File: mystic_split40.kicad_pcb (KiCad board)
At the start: 2 copper layers, 200.5 x 98.8 mm, 152 parts, among them J1 RX, J15 RESET, J16 ISP, J17 WS2812, J18 SJ-43514-SMT, J2 TX, J25 TYPE-C-31-M-12, J3 RX, J33 RESET, J34 ISP, J35 WS2812, J36 SJ-43514-SMT, J5 TX, J7 TYPE-C-31-M-12, SW1 EC11E, SW2 EC11E, SW3 Reset, SW4 Reset, U1 ATmega32U4-AU, U2 ATmega32U4-AU, Y1 CSTNE16M0VH3L000R0, Y2 CSTNE16M0VH3L000R0

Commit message: Swapped SDA and SCL pins on TRRS jack
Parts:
- removed C7, C8: 4.7nF, Capacitor_SMD:C_0603_1608Metric_Pad1.05x0.95mm_HandSolder
- removed R25, R26: 1M, Resistor_SMD:R_0603_1608Metric_Pad1.05x0.95mm_HandSolder
- added J4: F0, TestPoint:TestPoint_Pad_D1.0mm, B.Cu at (64.3, 21.5)
- added J6: F1, TestPoint:TestPoint_Pad_D1.0mm, B.Cu at (62.2, 21.5)
- added J8: F0, TestPoint:TestPoint_Pad_D1.0mm, B.Cu at (169.6, 21.5)
- added J9: F1, TestPoint:TestPoint_Pad_D1.0mm, B.Cu at (167.4, 21.5)
- moved R14 3.86 mm to (123.7, 21.0), turned to 270 degrees
- moved R13 3.83 mm to (120.8, 23.5), turned to 180 degrees
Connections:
- J25 pad S1: Net-(C8-Pad1) -> GND
- J7 pad S1: Net-(C7-Pad1) -> GND
- R13 pad 2: /Left MCU/SCL -> /Left MCU/SDA
- R14 pad 2: /Left MCU/SDA -> /Left MCU/SCL
- R23 pad 2: /Right MCU/SCL -> /Right MCU/SDA
- R24 pad 2: /Right MCU/SDA -> /Right MCU/SCL
- U1 pad 40: (no net) -> Net-(J6-Pad1)
- U1 pad 41: (no net) -> Net-(J4-Pad1)
- U2 pad 40: (no net) -> Net-(J9-Pad1)
- U2 pad 41: (no net) -> Net-(J8-Pad1)
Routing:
- net GND: track 81.4 -> 93.8 mm, vias 286 -> 330
- net Net-(J4-Pad1): track 0.00 -> 7.00 mm, vias 0 -> 1
- net Net-(J8-Pad1): track 0.00 -> 7.00 mm, vias 0 -> 1
- net /Left MCU/Rr_1: track 11.7 -> 17.5 mm, vias 1 -> 2
- net Net-(C7-Pad1): track 5.32 -> 0.00 mm
- net Net-(J6-Pad1): track 0.00 -> 4.81 mm, vias 0 -> 1
- net Net-(J9-Pad1): track 0.00 -> 4.81 mm, vias 0 -> 1
- net /Right MCU/SDA: track 30.9 -> 26.4 mm
- net Net-(C8-Pad1): track 3.59 -> 0.00 mm
- net /Right MCU/SCL: track 27.2 -> 28.8 mm
- net +5V: track 313.6 -> 315.2 mm
- net Net-(J7-PadA5): track 6.86 -> 8.07 mm
- net /Left MCU/SCL: track 59.1 -> 58.0 mm
- net /Left MCU/Rr_2: track 15.4 -> 16.0 mm
- removed copper zone on B.Cu, net Net-(C7-Pad1)
- removed copper zone on B.Cu, net Net-(C8-Pad1)

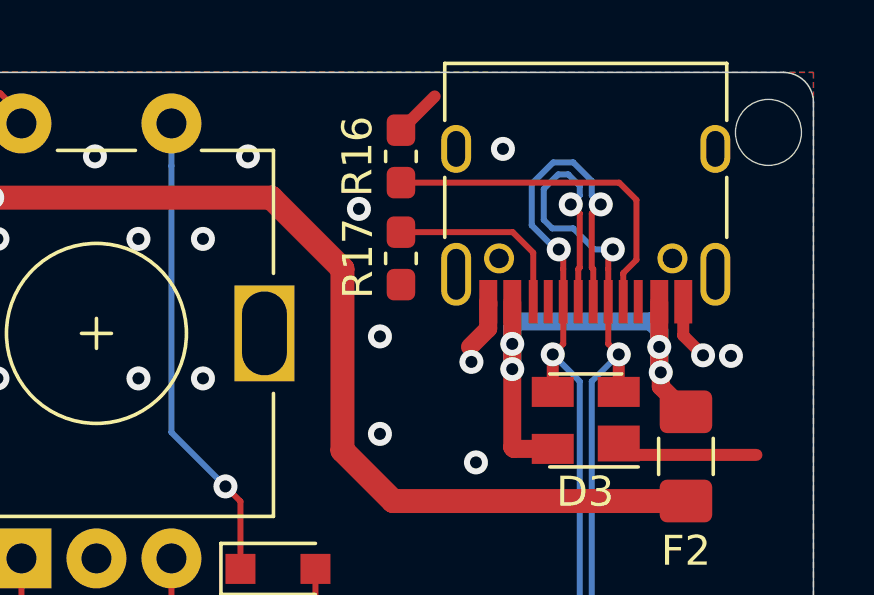
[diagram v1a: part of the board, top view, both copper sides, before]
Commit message: Changed right USB peg holes to solid pour connection
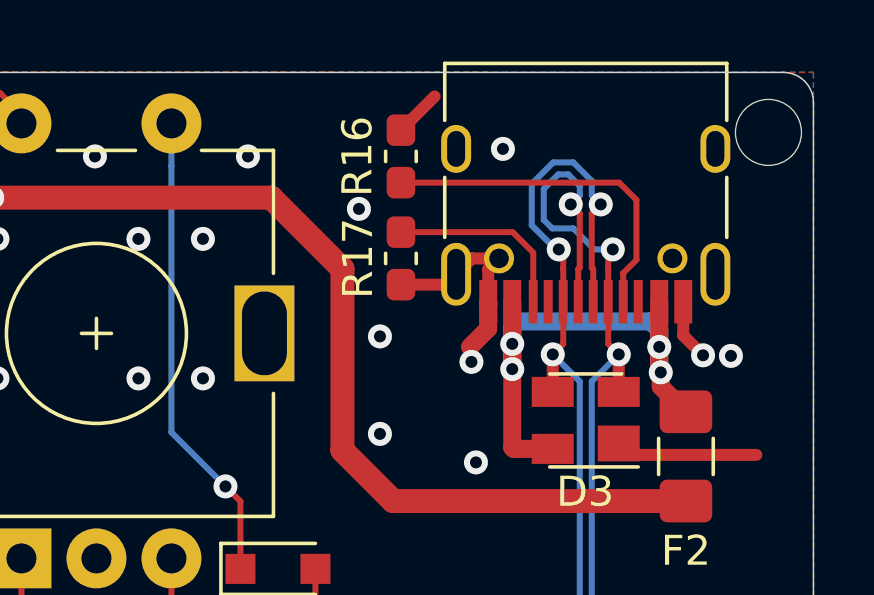
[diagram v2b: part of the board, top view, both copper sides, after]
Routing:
- net GND: track 93.8 -> 99.1 mm
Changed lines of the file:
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@@
     (thickness 1.6)
     (drawings 29)
-    (tracks 2348)
+    (tracks 2354)
     (zones 0)
     (modules 152)
@@
   )
   (setup
-    (last_trace_width 0.2)
+    (last_trace_width 0.4)
     (user_trace_width 0.4)
     (user_trace_width 0.6)
@@
     (mod_text_size 1 1)
     (mod_text_width 0.15)
-    (pad_size 1.05 1.05)
+    (pad_size 1 1)
     (pad_drill 0.65)
     (pad_to_mask_clearance 0.051)
@@
       (net 1 GND))
     (pad S1 thru_hole circle (at 2.89 -2.6 180) (size 1 1) (drill 0.65) (layers *.Cu *.Mask)
-      (net 1 GND))
+      (net 1 GND) (zone_connect 2))
     (pad S1 thru_hole oval (at -4.32 1.05 180) (size 1 1.6) (drill oval 0.6 1.2) (layers *.Cu *.Mask)
       (net 1 GND))
     (pad S1 thru_hole circle (at -2.89 -2.6 180) (size 1 1) (drill 0.65) (layers *.Cu *.Mask)
-      (net 1 GND))
+      (net 1 GND) (zone_connect 2))
     (pad S1 thru_hole oval (at -4.32 -3.13 180) (size 1 2.1) (drill oval 0.6 1.7) (layers *.Cu *.Mask)
       (net 1 GND))
@@
   (segment (start 159.375 27.9) (end 159.375 26.4) (width 0.6) (layer F.Cu) (net 1))
   (segment (start 195.125 19.05) (end 197.925 19.05) (width 0.6) (layer F.Cu) (net 1))
+  (segment (start 229.91 19.26) (end 230.27 18.9) (width 0.4) (layer F.Cu) (net 1))
+  (segment (start 229.91 20.345) (end 229.91 19.26) (width 0.4) (layer F.Cu) (net 1))
+  (segment (start 229.37 18.9) (end 228.84 19.43) (width 0.4) (layer F.Cu) (net 1))
+  (segment (start 230.27 18.9) (end 229.37 18.9) (width 0.4) (layer F.Cu) (net 1))
+  (segment (start 228.495 19.775) (end 228.84 19.43) (width 0.4) (layer F.Cu) (net 1))
+  (segment (start 227 19.775) (end 228.495 19.775) (width 0.4) (layer F.Cu) (net 1))
   (segment (start 102.175 15.025) (end 100.275 16.925) (width 0.2) (layer F.Cu) (net 2))
   (segment (start 100.275 16.925) (end 100.275 19.05) (width 0.2) (layer F.Cu) (net 2))

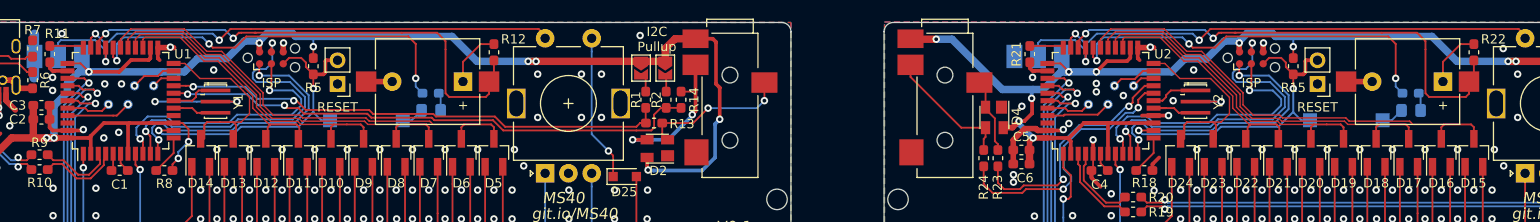
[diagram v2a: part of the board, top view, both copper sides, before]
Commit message: Improved ground routing from ISP header
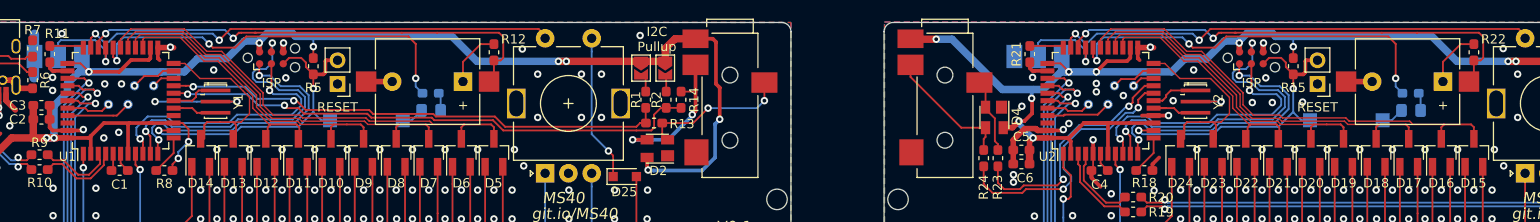
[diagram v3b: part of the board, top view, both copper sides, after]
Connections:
- SW1 pad MP: (no net) -> GND
- SW2 pad MP: (no net) -> GND
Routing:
- net /Left MCU/buzz: track 54.0 -> 51.5 mm
- net /Right MCU/buzz: track 54.0 -> 51.5 mm
- net GND: vias 330 -> 336

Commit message: regenerated gerbers
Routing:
- net +5V: vias 21 -> 22

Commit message: Started work on adding extra col
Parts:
- removed the G*** at (230.6, 32.9)
- removed the G*** at (125.3, 32.9)
- removed J4, J8: F0, TestPoint:TestPoint_Pad_D1.0mm
- removed MX19, MX24: MX-NoLED, Ai03-MX:MXOnly-1U-Hotswap
- removed MX43: MX-NoLED, Ai03-MX:MXOnly-2U-Hotswap
- removed the REF** at (147.0, 31.7)
- removed the REF** at (41.8, 14.7)
- removed the REF** at (97.4, 92.5)
- removed the REF** at (78.3, 92.5)
- removed the REF** at (116.5, 54.4)
- removed the REF** at (59.3, 54.4)
- removed the REF** at (239.2, 14.7)
- removed the REF** at (239.2, 31.7)
- removed the REF** at (202.7, 92.5)
- removed the REF** at (183.6, 92.5)
- removed the REF** at (221.7, 54.4)
- removed the REF** at (164.6, 54.4)
- removed the REF** at (134.0, 31.7)
- removed the REF** at (41.8, 31.7)
- added D29: PRTR5V0U2X, Package_TO_SOT_SMD:SOT-143, F.Cu at (26.6, 28.4)
- added D30: PRTR5V0U2X, Package_TO_SOT_SMD:SOT-143, F.Cu at (118.8, 30.4)
- added D31: BAV70, Diode_SMD:D_SOD-323_HandSoldering, F.Cu at (114.3, 33.7)
- added D32: Red LED, LED_SMD:LED_0805_2012Metric_Pad1.15x1.40mm_HandSolder, F.Cu at (94.2, 23.1)
- added G***: LOGO, graphics:kiwi10mm, B.Cu at (123.0, 37.0)
- added MX45: MX-NoLED, Ai03-MX:MXOnly-1U-Hotswap, F.Cu at (481.6, -5.21)
- added MX46: MX-NoLED, Ai03-MX:MXOnly-1U-Hotswap, F.Cu at (481.6, 15.0)
- added MX47: MX-NoLED, Ai03-MX:MXOnly-1U-Hotswap, F.Cu at (520.9, -25.4)
- added MXA19: MX-NoLED, Ai03-MX:MXOnly-1U-Hotswap, F.Cu at (28.4, 106.2)
- added MXA24: MX-NoLED, Ai03-MX:MXOnly-1U-Hotswap, F.Cu at (123.7, 106.2)
- added MXA43: MX-NoLED, Ai03-MX:MXOnly-1U-Hotswap, F.Cu at (501.8, -5.21)
- added MXA48: MX-NoLED, Ai03-MX:MXOnly-1U-Hotswap, F.Cu at (501.8, 15.0)
- added MXB19: MX-NoLED, Ai03-MX:MXOnly-2U-Hotswap, F.Cu at (38.0, 106.2)
- added MXB24: MX-NoLED, Ai03-MX:MXOnly-2U-Hotswap, F.Cu at (114.2, 106.2)
- added MXB43: MX-NoLED, Ai03-MX:MXOnly-2U-Hotswap, F.Cu at (410.4, -45.6)
- added MXB48: MX-NoLED, Ai03-MX:MXOnly-2U-Hotswap, F.Cu at (410.4, -24.8)
- added REF**: MountingHole_2.2mm_M2_DIN965, MountingHole:MountingHole_2.2mm_M2_DIN965, F.Cu at (131.7, 35.8)
- added REF**: MountingHole_2.2mm_M2_DIN965, MountingHole:MountingHole_2.2mm_M2_DIN965, F.Cu at (20.4, 35.8)
- added REF**: MountingHole_2.2mm_M2_DIN965, MountingHole:MountingHole_2.2mm_M2_DIN965, F.Cu at (20.4, 18.8)
- added REF**: MountingHole_3.2mm_M3_DIN965_Pad, MountingHole:MountingHole_3.2mm_M3_DIN965_Pad, F.Cu at (95.1, 96.6)
- added REF**: MountingHole_3.2mm_M3_DIN965_Pad, MountingHole:MountingHole_3.2mm_M3_DIN965_Pad, F.Cu at (57.0, 96.6)
- added REF**: MountingHole_3.2mm_M3_DIN965_Pad, MountingHole:MountingHole_3.2mm_M3_DIN965_Pad, F.Cu at (114.2, 58.5)
- added REF**: MountingHole_3.2mm_M3_DIN965_Pad, MountingHole:MountingHole_3.2mm_M3_DIN965_Pad, F.Cu at (38.0, 58.5)
- added TP1: SCK, TestPoint:TestPoint_Pad_D1.0mm, F.Cu at (122.9, -42.2)
- added TP2: MOSI, TestPoint:TestPoint_Pad_D1.0mm, F.Cu at (126.0, -42.2)
- added TP3: MISO, TestPoint:TestPoint_Pad_D1.0mm, F.Cu at (129.0, -42.2)
- added TP4: SCK, TestPoint:TestPoint_Pad_D1.0mm, B.Cu at (70.0, 22.3)
- added TP5: MOSI, TestPoint:TestPoint_Pad_D1.0mm, B.Cu at (67.8, 22.3)
- added TP6: MISO, TestPoint:TestPoint_Pad_D1.0mm, B.Cu at (72.2, 22.3)
- D25, D26: footprint Diode_SMD:D_SOD-323_HandSoldering -> Package_TO_SOT_SMD:SOT-23_Handsoldering
- D27: value Red LED -> BAV70; footprint LED_SMD:LED_0805_2012Metric_Pad1.15x1.40mm_HandSolder -> Diode_SMD:D_SOD-323_HandSoldering; moved to F.Cu
- D28, J3, J35, J5, J9, R3, R4, SW4: moved to F.Cu
- D3, D4: value PRTR5V0U2X -> BAV70; footprint Package_TO_SOT_SMD:SOT-143 -> Package_TO_SOT_SMD:SOT-23_Handsoldering
- MX41, MX42, MX44: footprint Ai03-MX:MXOnly-2U-Hotswap -> Ai03-MX:MXOnly-1U-Hotswap
- moved MX41 404.8 mm to (500.7, -25.4), turned to 0 degrees
- moved D1 374.1 mm to (419.9, 64.1), turned to 0 degrees
- moved D22 358.9 mm to (534.2, -53.4), turned to 0 degrees
- moved MX27 351.4 mm to (522.0, 15.0)
- moved MX38 341.1 mm to (500.7, -45.6)
- moved MX26 337.5 mm to (480.5, -25.4)
- moved MX42 333.6 mm to (520.9, -45.6), turned to 0 degrees
- moved D2 326.1 mm to (447.0, 39.1), turned to 0 degrees
- moved MX44 309.4 mm to (461.4, 15.0), turned to 0 degrees
- moved MX36 305.6 mm to (441.2, -5.21)
- moved MX37 304.2 mm to (440.1, -45.6)
- moved MX35 303.9 mm to (522.0, -5.21)
- moved MX34 297.5 mm to (480.5, -45.6)
- moved R24 290.8 mm to (446.6, 42.6), turned to 0 degrees
- moved MX33 288.3 mm to (460.3, -25.4)
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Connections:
- D1 pad 2: /Left MCU/Dd- -> /Right MCU/Dd-
- D1 pad 3: /Left MCU/Dd+ -> /Right MCU/Dd+
- D15 pad 3: /Matrix right/col4 -> /Matrix right/col5
- D16 pad 3: /Matrix right/col4 -> /Matrix right/col5
- D17 pad 3: /Matrix right/col3 -> /Matrix right/col4
- D18 pad 3: /Matrix right/col3 -> /Matrix right/col4
- D19 pad 3: /Matrix right/col2 -> /Matrix right/col3
- D2 pad 2: /Left MCU/Rr_2 -> /Right MCU/Rr_2
- D2 pad 3: /Left MCU/Rr_1 -> /Right MCU/Rr_1
- D20 pad 3: /Matrix right/col2 -> /Matrix right/col3
- D21 pad 3: /Matrix right/col1 -> /Matrix right/col2
- D22 pad 3: /Matrix right/col1 -> /Matrix right/col2
- D23 pad 3: /Matrix right/col0 -> /Matrix right/col1
- D24 pad 3: /Matrix right/col0 -> /Matrix right/col1
- D25 pad 2: /Left MCU/row0 -> Net-(D25-Pad2)
- D26 pad 2: /Matrix right/row0 -> Net-(D26-Pad2)
- D27 pad 1: GND -> Net-(D27-Pad1)
- D27 pad 2: Net-(D27-Pad2) -> /Matrix right/row0
- D3 pad 1: GND -> Net-(D3-Pad1)
- D3 pad 2: /Right MCU/Dd- -> Net-(D3-Pad2)
- D3 pad 3: /Right MCU/Dd+ -> /Left MCU/col5
- D4 pad 1: GND -> Net-(D4-Pad1)
- D4 pad 2: /Right MCU/Rr_2 -> Net-(D4-Pad2)
- D4 pad 3: /Right MCU/Rr_1 -> /Left MCU/col5
- MX10 pad 1: Net-(D5-Pad1) -> Net-(D7-Pad1)
- MX11 pad 1: Net-(D14-Pad2) -> Net-(D5-Pad1)
- MX11 pad 2: /Left MCU/row2 -> /Left MCU/row1
- MX12 pad 1: Net-(D12-Pad2) -> Net-(D3-Pad1)
- MX12 pad 2: /Left MCU/row2 -> /Left MCU/row1
- MX13 pad 1: Net-(D10-Pad2) -> Net-(D14-Pad2)
- MX14 pad 1: Net-(D8-Pad2) -> Net-(D12-Pad2)
- MX15 pad 1: Net-(D6-Pad2) -> Net-(D10-Pad2)
- MX16 pad 1: Net-(D14-Pad1) -> Net-(D8-Pad2)
- MX16 pad 2: /Left MCU/row3 -> /Left MCU/row2
- MX17 pad 1: Net-(D12-Pad1) -> Net-(D6-Pad2)
- MX17 pad 2: /Left MCU/row3 -> /Left MCU/row2
- MX18 pad 1: Net-(D10-Pad1) -> Net-(D4-Pad2)
- MX18 pad 2: /Left MCU/row3 -> /Left MCU/row2
- MX20 pad 1: Net-(D6-Pad1) -> Net-(D12-Pad1)
- MX21 pad 1: Net-(D23-Pad2) -> Net-(D10-Pad1)
- MX21 pad 2: /Matrix right/row0 -> /Left MCU/row3
- MX22 pad 1: Net-(D21-Pad2) -> Net-(D8-Pad1)
- MX22 pad 2: /Matrix right/row0 -> /Left MCU/row3
- MX23 pad 1: Net-(D19-Pad2) -> Net-(D6-Pad1)
- MX23 pad 2: /Matrix right/row0 -> /Left MCU/row3
- MX25 pad 1: Net-(D15-Pad2) -> Net-(D25-Pad2)
- MX26 pad 1: Net-(D23-Pad1) -> Net-(D23-Pad2)
- MX26 pad 2: /Matrix right/row1 -> /Matrix right/row0
- MX27 pad 1: Net-(D21-Pad1) -> Net-(D21-Pad2)
- MX27 pad 2: /Matrix right/row1 -> /Matrix right/row0
- MX28 pad 1: Net-(D19-Pad1) -> Net-(D19-Pad2)
- MX28 pad 2: /Matrix right/row1 -> /Matrix right/row0
- MX29 pad 1: Net-(D17-Pad1) -> Net-(D17-Pad2)
- MX29 pad 2: /Matrix right/row1 -> /Matrix right/row0
- MX30 pad 1: Net-(D15-Pad1) -> Net-(D15-Pad2)
- MX30 pad 2: /Matrix right/row1 -> /Matrix right/row0
- MX31 pad 1: Net-(D24-Pad2) -> Net-(D25-Pad1)
- MX31 pad 2: /Matrix right/row2 -> /Matrix right/row1
- MX32 pad 1: Net-(D22-Pad2) -> Net-(D23-Pad1)
- MX32 pad 2: /Matrix right/row2 -> /Matrix right/row1
- MX33 pad 1: Net-(D20-Pad2) -> Net-(D21-Pad1)
- MX33 pad 2: /Matrix right/row2 -> /Matrix right/row1
- MX34 pad 1: Net-(D18-Pad2) -> Net-(D19-Pad1)
- MX34 pad 2: /Matrix right/row2 -> /Matrix right/row1
- MX35 pad 1: Net-(D16-Pad2) -> Net-(D17-Pad1)
- MX35 pad 2: /Matrix right/row2 -> /Matrix right/row1
- MX36 pad 1: Net-(D24-Pad1) -> Net-(D15-Pad1)
- MX36 pad 2: /Matrix right/row3 -> /Matrix right/row1
- MX37 pad 1: Net-(D22-Pad1) -> Net-(D26-Pad2)
- MX37 pad 2: /Matrix right/row3 -> /Matrix right/row2
- MX38 pad 1: Net-(D20-Pad1) -> Net-(D24-Pad2)
- MX38 pad 2: /Matrix right/row3 -> /Matrix right/row2
- MX39 pad 1: Net-(D18-Pad1) -> Net-(D22-Pad2)
- MX39 pad 2: /Matrix right/row3 -> /Matrix right/row2
- MX40 pad 1: Net-(D16-Pad1) -> Net-(D20-Pad2)
- MX40 pad 2: /Matrix right/row3 -> /Matrix right/row2
- MX41 pad 1: Net-(D6-Pad1) -> Net-(D18-Pad2)
- MX41 pad 2: /Left MCU/row3 -> /Matrix right/row2
- MX42 pad 1: Net-(D16-Pad1) -> Net-(D16-Pad2)
- MX42 pad 2: /Matrix right/row3 -> /Matrix right/row2
- MX6 pad 1: Net-(D13-Pad1) -> Net-(D3-Pad2)
- MX6 pad 2: /Left MCU/row1 -> /Left MCU/row0
- MX7 pad 1: Net-(D11-Pad1) -> Net-(D13-Pad1)
- MX8 pad 1: Net-(D9-Pad1) -> Net-(D11-Pad1)
- MX9 pad 1: Net-(D7-Pad1) -> Net-(D9-Pad1)
- R3 pad 1: Net-(D27-Pad2) -> Net-(D32-Pad2)
- SW1 pad S1: Net-(D25-Pad1) -> Net-(D31-Pad1)
- SW2 pad MP: GND -> (no net)
- SW2 pad S1: Net-(D26-Pad1) -> Net-(D27-Pad1)
- U1 pad 29: /Left MCU/DFU_LED -> /Left MCU/col5
- U1 pad 41: Net-(J4-Pad1) -> /Left MCU/DFU_LED
- U2 pad 29: /Right MCU/DFU_LED -> /Matrix right/col5
- U2 pad 41: Net-(J8-Pad1) -> /Right MCU/DFU_LED
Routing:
- net /Matrix right/row3: track 193.6 -> 0.00 mm, vias 3 -> 0
- net /Matrix right/row2: track 148.1 -> 0.00 mm, vias 3 -> 0
- net /Matrix right/row1: track 133.4 -> 0.00 mm, vias 3 -> 0
- net +5V: track 315.2 -> 187.7 mm, vias 22 -> 7
- net /Matrix right/row0: track 118.2 -> 0.00 mm, vias 2 -> 0
- net Net-(D24-Pad1): track 114.2 -> 0.00 mm, vias 1 -> 0
- net Net-(D4-Pad1): track 0.00 -> 110.3 mm, vias 0 -> 1
- net Net-(D16-Pad1): track 105.0 -> 0.00 mm, vias 1 -> 0
- net Net-(D22-Pad1): track 91.6 -> 0.00 mm, vias 1 -> 0
- net /Right MCU/Dd-: track 85.2 -> 0.00 mm, vias 4 -> 0
- net /Right MCU/Dd+: track 84.5 -> 0.00 mm, vias 4 -> 0
- net Net-(D24-Pad2): track 81.7 -> 0.00 mm, vias 1 -> 0
- net Net-(D20-Pad1): track 77.4 -> 0.00 mm, vias 1 -> 0
- net Net-(D4-Pad2): track 0.00 -> 76.3 mm, vias 0 -> 1
- net Net-(D18-Pad1): track 75.3 -> 0.00 mm, vias 1 -> 0
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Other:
- board size 200.5 x 98.8 mm -> 114.3 x 98.8 mm
- board text added: "V0.2.0"
- board text removed: "+ D -"
- board text removed: "V0.1"

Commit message: Changed version silk
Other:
- board text added: "V0.3.0"
- board text removed: "V0.2.0"
